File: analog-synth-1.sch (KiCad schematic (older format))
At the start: 0 parts

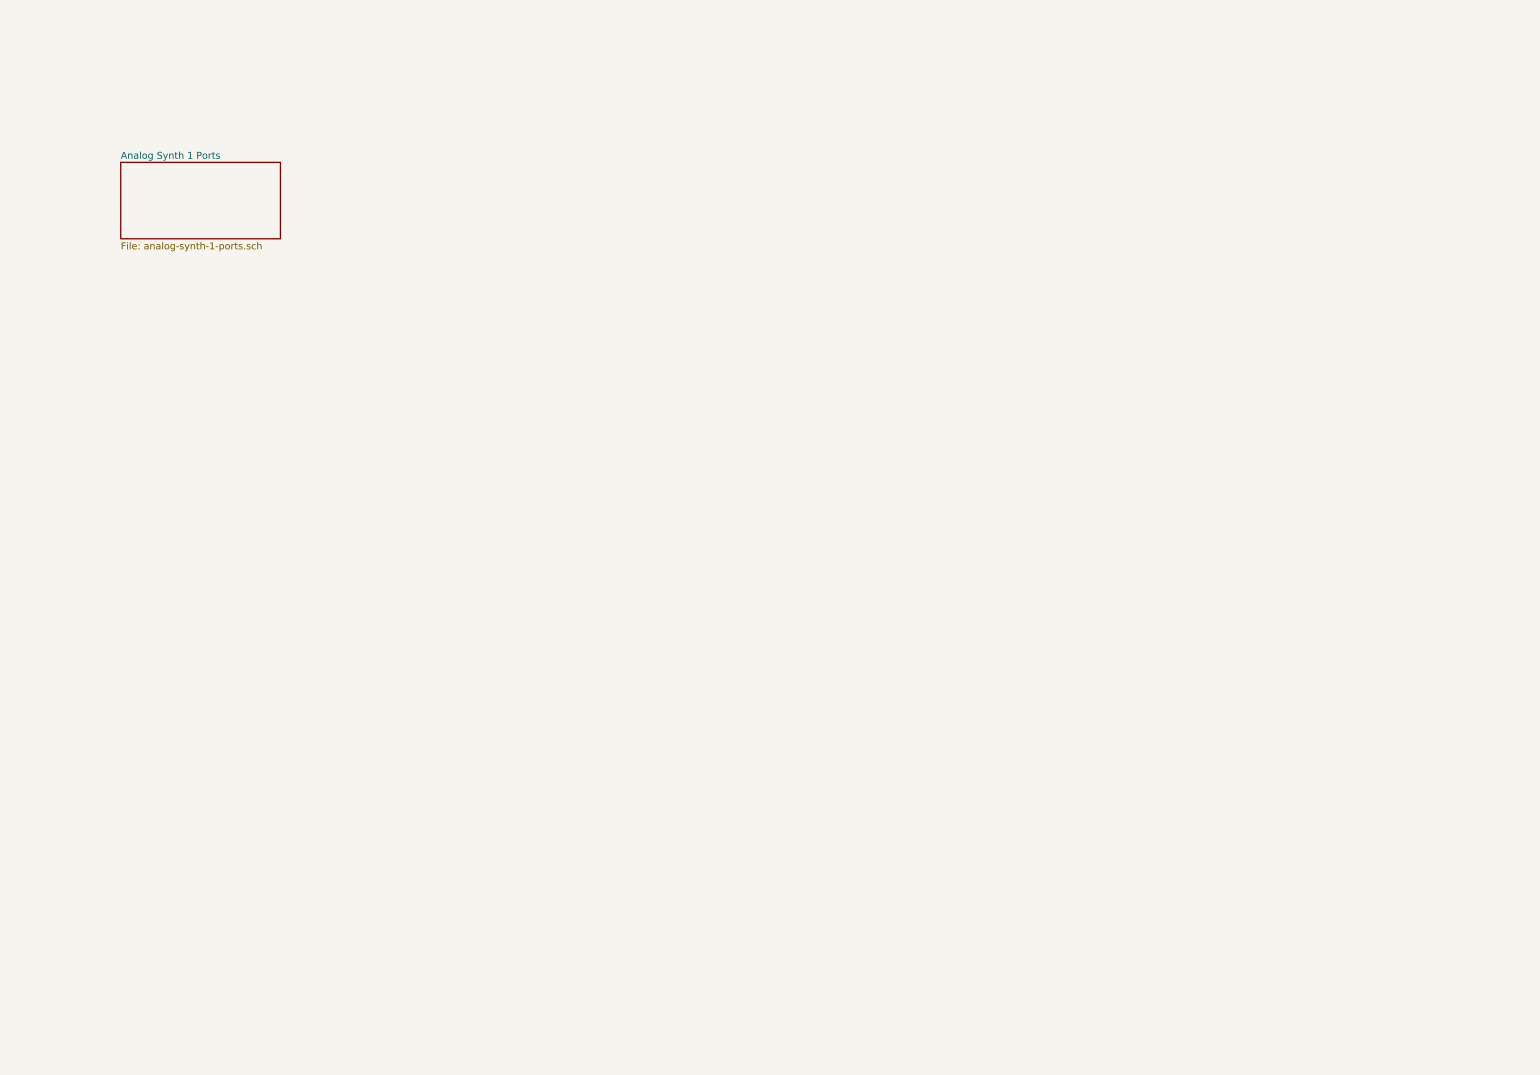
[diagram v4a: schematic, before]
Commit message: Finish basic synth circuit diagram
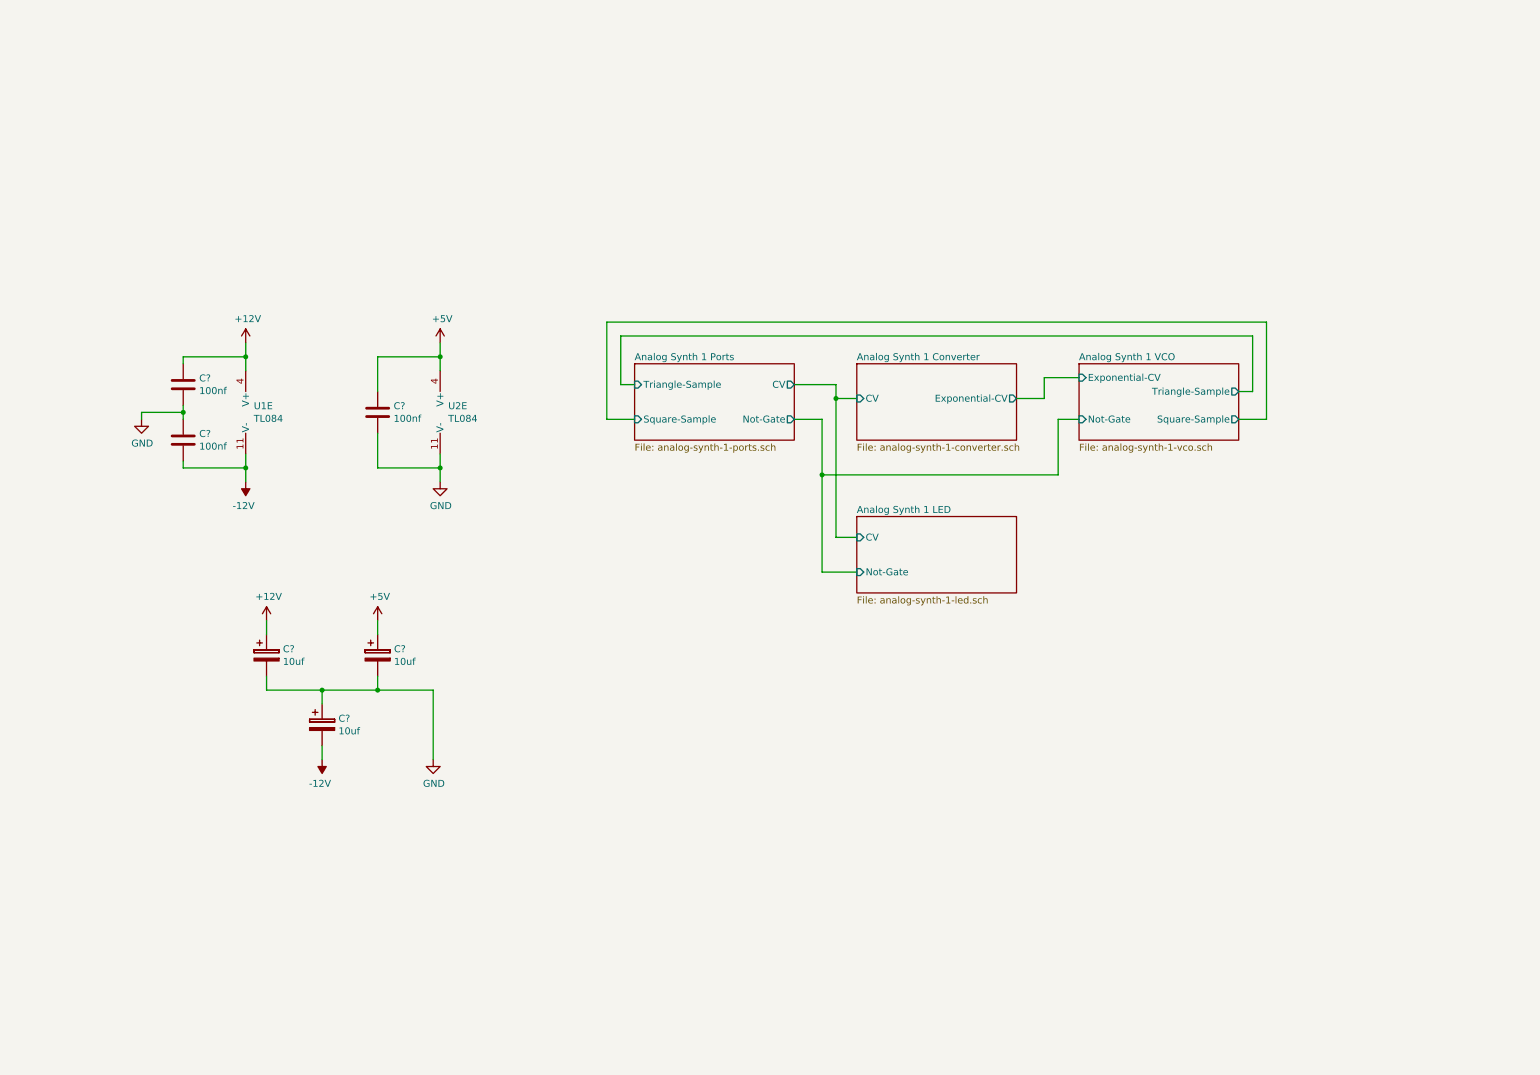
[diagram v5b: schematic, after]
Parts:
- added C? (x3): 100nf, symbol Device:C
- added C? (x3): 10uf, symbol Device:CP
- added U1, U2: TL084, symbol Amplifier_Operational:TL084
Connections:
- new net +12V: C?.1, C?.1, U1.4 (V+)
- new net +5V: C?.1, C?.1, U2.4 (V+)
- new net -12V: C?.2, C?.2, U1.11 (V-)
- new net GND: C?.1, C?.1, C?.2, C?.2, C?.2, C?.2, U2.11 (V-)

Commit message: Annotate components
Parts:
- gave numbers to parts that had none: 6
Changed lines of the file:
@@
 $EndComp
 $Comp
-L power:+12V #PWR?
+L power:+12V #PWR02
 U 1 1 5C8A06B3
 P 2250 2700
-F 0 "#PWR?" H 2250 2550 50  0001 C CNN
+F 0 "#PWR02" H 2250 2550 50  0001 C CNN
 F 1 "+12V" H 2265 2873 50  0000 C CNN
 F 2 "" H 2250 2700 50  0001 C CNN
@@
 	2250 2700 2250 2800
 $Comp
-L power:-12V #PWR?
+L power:-12V #PWR03
 U 1 1 5C8A0733
 P 2250 3700
-F 0 "#PWR?" H 2250 3800 50  0001 C CNN
+F 0 "#PWR03" H 2250 3800 50  0001 C CNN
 F 1 "-12V" H 2265 3873 50  0000 C CNN
 F 2 "" H 2250 3700 50  0001 C CNN
@@
 	2250 3700 2250 3600
 $Comp
-L power:GND #PWR?
+L power:GND #PWR09
 U 1 1 5C8A07A5
 P 3650 3700
-F 0 "#PWR?" H 3650 3450 50  0001 C CNN
+F 0 "#PWR09" H 3650 3450 50  0001 C CNN
 F 1 "GND" H 3655 3527 50  0000 C CNN
 F 2 "" H 3650 3700 50  0001 C CNN
@@
 $EndComp
 $Comp
-L power:+5V #PWR?
+L power:+5V #PWR08
 U 1 1 5C8A0819
 P 3650 2700
-F 0 "#PWR?" H 3650 2550 50  0001 C CNN
+F 0 "#PWR08" H 3650 2550 50  0001 C CNN
 F 1 "+5V" H 3665 2873 50  0000 C CNN
 F 2 "" H 3650 2700 50  0001 C CNN
@@
 $EndComp
 $Comp
-L Device:C C?
+L Device:C C1
 U 1 1 5C8A08B9
 P 1800 3000
-F 0 "C?" H 1915 3046 50  0000 L CNN
+F 0 "C1" H 1915 3046 50  0000 L CNN
 F 1 "100nf" H 1915 2955 50  0000 L CNN
 F 2 "" H 1838 2850 50  0001 C CNN
@@
 $EndComp
 $Comp
-L Device:C C?
+L Device:C C2
 U 1 1 5C8A08FC
 P 1800 3400
-F 0 "C?" H 1915 3446 50  0000 L CNN
+F 0 "C2" H 1915 3446 50  0000 L CNN
 F 1 "100nf" H 1915 3355 50  0000 L CNN
 F 2 "" H 1838 3250 50  0001 C CNN
@@
 	2250 3600 2250 3500
 $Comp
-L power:GND #PWR?
+L power:GND #PWR01
 U 1 1 5C8A0ABB
 P 1500 3250
-F 0 "#PWR?" H 1500 3000 50  0001 C CNN
+F 0 "#PWR01" H 1500 3000 50  0001 C CNN
 F 1 "GND" H 1505 3077 50  0000 C CNN
 F 2 "" H 1500 3250 50  0001 C CNN
@@
 	1800 3200 1800 3250
 $Comp
-L Device:C C?
+L Device:C C5
 U 1 1 5C8A0BD8
 P 3200 3200
-F 0 "C?" H 3315 3246 50  0000 L CNN
+F 0 "C5" H 3315 3246 50  0000 L CNN
 F 1 "100nf" H 3315 3155 50  0000 L CNN
 F 2 "" H 3238 3050 50  0001 C CNN
@@
 	3650 3600 3650 3700
 $Comp
-L power:+12V #PWR?
+L power:+12V #PWR04
 U 1 1 5C8A2596
 P 2400 4700
-F 0 "#PWR?" H 2400 4550 50  0001 C CNN
+F 0 "#PWR04" H 2400 4550 50  0001 C CNN
 F 1 "+12V" H 2415 4873 50  0000 C CNN
 F 2 "" H 2400 4700 50  0001 C CNN
@@
 $EndComp
 $Comp
-L power:+5V #PWR?
+L power:+5V #PWR06
 U 1 1 5C8A25DD
 P 3200 4700
-F 0 "#PWR?" H 3200 4550 50  0001 C CNN
+F 0 "#PWR06" H 3200 4550 50  0001 C CNN
 F 1 "+5V" H 3215 4873 50  0000 C CNN
 F 2 "" H 3200 4700 50  0001 C CNN
@@
 $EndComp
 $Comp
-L Device:CP C?
+L Device:CP C6
 U 1 1 5C8A292F
 P 3200 4950
-F 0 "C?" H 3318 4996 50  0000 L CNN
+F 0 "C6" H 3318 4996 50  0000 L CNN
 F 1 "10uf" H 3318 4905 50  0000 L CNN
 F 2 "" H 3238 4800 50  0001 C CNN
@@
 $EndComp
 $Comp
-L Device:CP C?
+L Device:CP C3
 U 1 1 5C8A2973
 P 2400 4950
-F 0 "C?" H 2518 4996 50  0000 L CNN
+F 0 "C3" H 2518 4996 50  0000 L CNN
 F 1 "10uf" H 2518 4905 50  0000 L CNN
 F 2 "" H 2438 4800 50  0001 C CNN
@@
 	3200 5200 3200 5100
 $Comp
-L Device:CP C?
+L Device:CP C4
 U 1 1 5C8A3250
 P 2800 5450
-F 0 "C?" H 2918 5496 50  0000 L CNN
+F 0 "C4" H 2918 5496 50  0000 L CNN
 F 1 "10uf" H 2918 5405 50  0000 L CNN
 F 2 "" H 2838 5300 50  0001 C CNN
@@
 	2800 5200 3200 5200
 $Comp
-L power:-12V #PWR?
+L power:-12V #PWR05
 U 1 1 5C8A3697
 P 2800 5700
-F 0 "#PWR?" H 2800 5800 50  0001 C CNN
+F 0 "#PWR05" H 2800 5800 50  0001 C CNN
 F 1 "-12V" H 2815 5873 50  0000 C CNN
 F 2 "" H 2800 5700 50  0001 C CNN
@@
 	2800 5700 2800 5600
 $Comp
-L power:GND #PWR?
+L power:GND #PWR07
 U 1 1 5C8A3B5D
 P 3600 5700
-F 0 "#PWR?" H 3600 5450 50  0001 C CNN
+F 0 "#PWR07" H 3600 5450 50  0001 C CNN
 F 1 "GND" H 3605 5527 50  0000 C CNN
 F 2 "" H 3600 5700 50  0001 C CNN

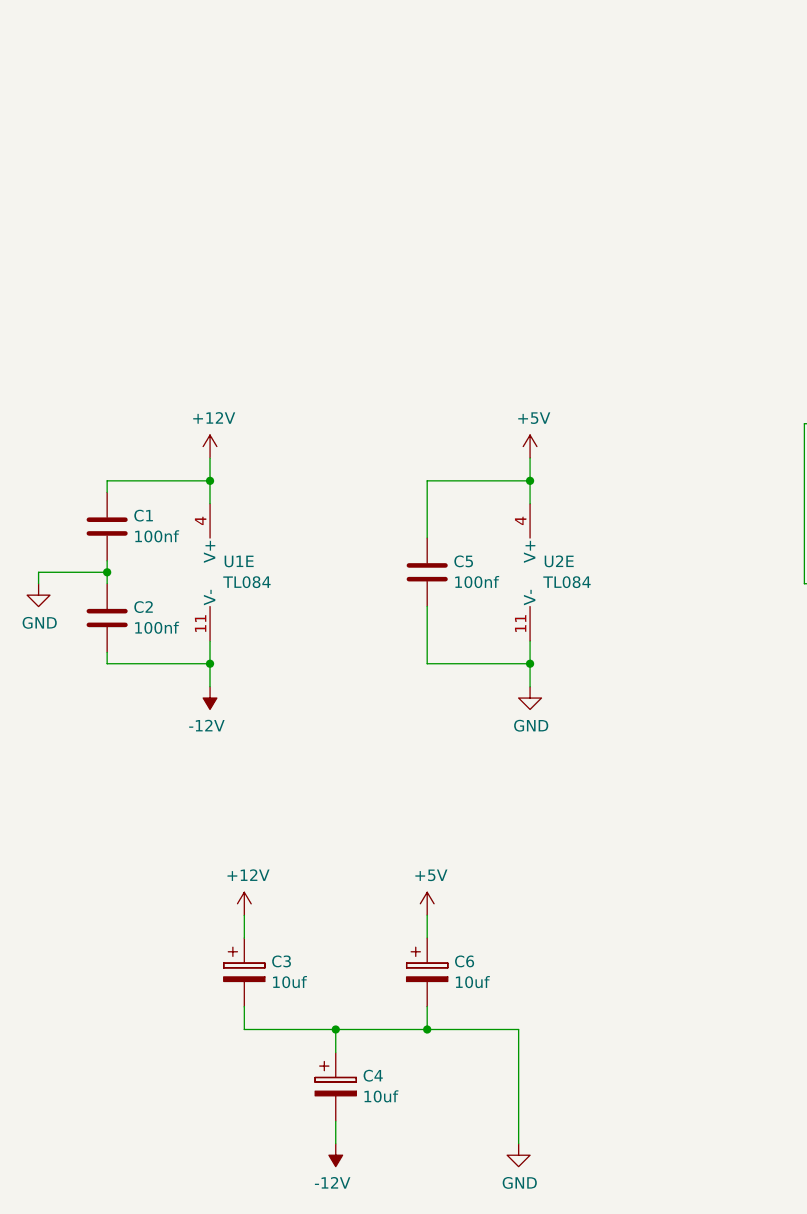
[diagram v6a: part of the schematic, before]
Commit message: Add ATtiny85 overdrive protection, fix #5
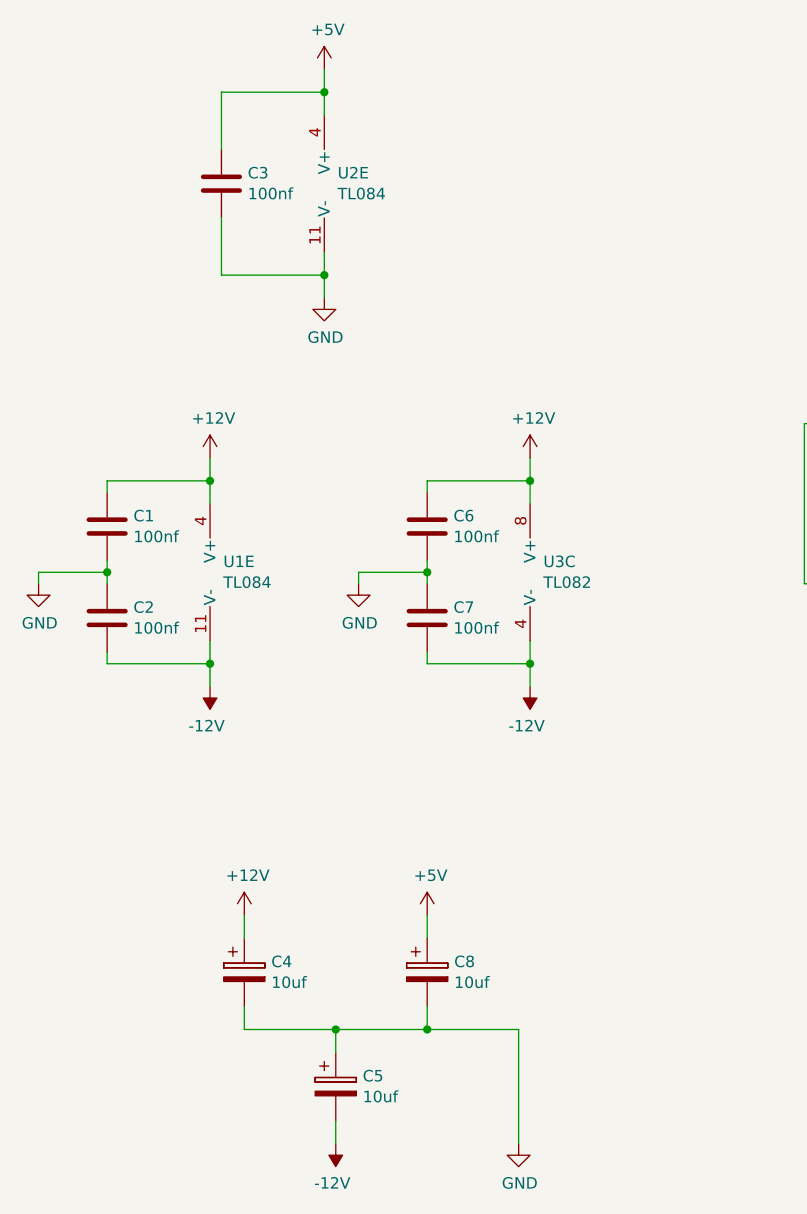
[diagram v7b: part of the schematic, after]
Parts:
- added C6, C7: 100nf, symbol Device:C
- added U3: TL082, symbol Amplifier_Operational:TL082
- renumbered C5 to C3, C3 to C4, C4 to C5, C6 to C8
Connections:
- net +12V: now also C6.1, U3.8 (V+)
- net -12V: now also C7.2, U3.4 (V-)
- net GND: now also C6.2, C7.1
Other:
- moved on the sheet: C3, U2E
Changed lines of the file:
@@
 L Amplifier_Operational:TL084 U2
 U 5 1 5C8A05FF
-P 3750 3200
-F 0 "U2" H 3708 3246 50  0000 L CNN
-F 1 "TL084" H 3708 3155 50  0000 L CNN
-F 2 "" H 3700 3300 50  0001 C CNN
-F 3 "http://www.ti.com/lit/ds/symlink/tl081.pdf" H 3800 3400 50  0001 C CNN
-	5    3750 3200
+P 2850 1500
+F 0 "U2" H 2808 1546 50  0000 L CNN
+F 1 "TL084" H 2808 1455 50  0000 L CNN
+F 2 "" H 2800 1600 50  0001 C CNN
+F 3 "http://www.ti.com/lit/ds/symlink/tl081.pdf" H 2900 1700 50  0001 C CNN
+	5    2850 1500
 	1    0    0    -1
 $EndComp
@@
 	2250 3700 2250 3600
 $Comp
-L power:GND #PWR09
+L power:GND #PWR06
 U 1 1 5C8A07A5
-P 3650 3700
-F 0 "#PWR09" H 3650 3450 50  0001 C CNN
-F 1 "GND" H 3655 3527 50  0000 C CNN
-F 2 "" H 3650 3700 50  0001 C CNN
-F 3 "" H 3650 3700 50  0001 C CNN
-	1    3650 3700
-	1    0    0    -1
-$EndComp
-$Comp
-L power:+5V #PWR08
+P 2750 2000
+F 0 "#PWR06" H 2750 1750 50  0001 C CNN
+F 1 "GND" H 2755 1827 50  0000 C CNN
+F 2 "" H 2750 2000 50  0001 C CNN
+F 3 "" H 2750 2000 50  0001 C CNN
+	1    2750 2000
+	1    0    0    -1
+$EndComp
+$Comp
+L power:+5V #PWR05
 U 1 1 5C8A0819
-P 3650 2700
-F 0 "#PWR08" H 3650 2550 50  0001 C CNN
-F 1 "+5V" H 3665 2873 50  0000 C CNN
-F 2 "" H 3650 2700 50  0001 C CNN
-F 3 "" H 3650 2700 50  0001 C CNN
-	1    3650 2700
+P 2750 1000
+F 0 "#PWR05" H 2750 850 50  0001 C CNN
+F 1 "+5V" H 2765 1173 50  0000 C CNN
+F 2 "" H 2750 1000 50  0001 C CNN
+F 3 "" H 2750 1000 50  0001 C CNN
+	1    2750 1000
 	1    0    0    -1
 $EndComp
@@
 	1800 3200 1800 3250
 $Comp
-L Device:C C5
+L Device:C C3
 U 1 1 5C8A0BD8
-P 3200 3200
-F 0 "C5" H 3315 3246 50  0000 L CNN
-F 1 "100nf" H 3315 3155 50  0000 L CNN
-F 2 "" H 3238 3050 50  0001 C CNN
-F 3 "~" H 3200 3200 50  0001 C CNN
-	1    3200 3200
-	1    0    0    -1
-$EndComp
-Wire Wire Line
-	3200 3050 3200 2800
-Wire Wire Line
-	3200 3350 3200 3600
-Wire Wire Line
-	3650 2700 3650 2800
-Wire Wire Line
-	3650 3500 3650 3600
-Wire Wire Line
-	3650 2800 3200 2800
-Connection ~ 3650 2800
-Wire Wire Line
-	3650 2800 3650 2900
-Wire Wire Line
-	3650 3600 3200 3600
-Connection ~ 3650 3600
-Wire Wire Line
-	3650 3600 3650 3700
+P 2300 1500
+F 0 "C3" H 2415 1546 50  0000 L CNN
+F 1 "100nf" H 2415 1455 50  0000 L CNN
+F 2 "" H 2338 1350 50  0001 C CNN
+F 3 "~" H 2300 1500 50  0001 C CNN
+	1    2300 1500
+	1    0    0    -1
+$EndComp
+Wire Wire Line
+	2300 1350 2300 1100
+Wire Wire Line
+	2300 1650 2300 1900
+Wire Wire Line
+	2750 1000 2750 1100
+Wire Wire Line
+	2750 1800 2750 1900
+Wire Wire Line
+	2750 1100 2300 1100
+Connection ~ 2750 1100
+Wire Wire Line
+	2750 1100 2750 1200
+Wire Wire Line
+	2750 1900 2300 1900
+Connection ~ 2750 1900
+Wire Wire Line
+	2750 1900 2750 2000
 $Comp
 L power:+12V #PWR04
@@
 $EndComp
 $Comp
-L power:+5V #PWR06
+L power:+5V #PWR09
 U 1 1 5C8A25DD
 P 3200 4700
-F 0 "#PWR06" H 3200 4550 50  0001 C CNN
+F 0 "#PWR09" H 3200 4550 50  0001 C CNN
 F 1 "+5V" H 3215 4873 50  0000 C CNN
 F 2 "" H 3200 4700 50  0001 C CNN
@@
 $EndComp
 $Comp
-L Device:CP C6
+L Device:CP C8
 U 1 1 5C8A292F
 P 3200 4950
-F 0 "C6" H 3318 4996 50  0000 L CNN
+F 0 "C8" H 3318 4996 50  0000 L CNN
 F 1 "10uf" H 3318 4905 50  0000 L CNN
 F 2 "" H 3238 4800 50  0001 C CNN
@@
 $EndComp
 $Comp
-L Device:CP C3
+L Device:CP C4
 U 1 1 5C8A2973
 P 2400 4950
-F 0 "C3" H 2518 4996 50  0000 L CNN
+F 0 "C4" H 2518 4996 50  0000 L CNN
 F 1 "10uf" H 2518 4905 50  0000 L CNN
 F 2 "" H 2438 4800 50  0001 C CNN
@@
 	3200 5200 3200 5100
 $Comp
-L Device:CP C4
+L Device:CP C5
 U 1 1 5C8A3250
 P 2800 5450
-F 0 "C4" H 2918 5496 50  0000 L CNN
+F 0 "C5" H 2918 5496 50  0000 L CNN
 F 1 "10uf" H 2918 5405 50  0000 L CNN
 F 2 "" H 2838 5300 50  0001 C CNN
@@
 	2800 5200 3200 5200
 $Comp
-L power:-12V #PWR05
+L power:-12V #PWR07
 U 1 1 5C8A3697
 P 2800 5700
-F 0 "#PWR05" H 2800 5800 50  0001 C CNN
+F 0 "#PWR07" H 2800 5800 50  0001 C CNN
 F 1 "-12V" H 2815 5873 50  0000 C CNN
 F 2 "" H 2800 5700 50  0001 C CNN
@@
 	2800 5700 2800 5600
 $Comp
-L power:GND #PWR07
+L power:GND #PWR010
 U 1 1 5C8A3B5D
 P 3600 5700
-F 0 "#PWR07" H 3600 5450 50  0001 C CNN
+F 0 "#PWR010" H 3600 5450 50  0001 C CNN
 F 1 "GND" H 3605 5527 50  0000 C CNN
 F 2 "" H 3600 5700 50  0001 C CNN
@@
 	6400 4350 6650 4350
 Connection ~ 6400 3650
+$Comp
+L power:+12V #PWR011
+U 1 1 5CA1F7C2
+P 3650 2700
+F 0 "#PWR011" H 3650 2550 50  0001 C CNN
+F 1 "+12V" H 3665 2873 50  0000 C CNN
+F 2 "" H 3650 2700 50  0001 C CNN
+F 3 "" H 3650 2700 50  0001 C CNN
+	1    3650 2700
+	1    0    0    -1
+$EndComp
+Wire Wire Line
+	3650 2700 3650 2800
+$Comp
+L power:-12V #PWR012
+U 1 1 5CA1F7C9
+P 3650 3700
+F 0 "#PWR012" H 3650 3800 50  0001 C CNN
+F 1 "-12V" H 3665 3873 50  0000 C CNN
+F 2 "" H 3650 3700 50  0001 C CNN
+F 3 "" H 3650 3700 50  0001 C CNN
+	1    3650 3700
+	-1   0    0    1
+$EndComp
+Wire Wire Line
+	3650 3700 3650 3600
+$Comp
+L Device:C C6
+U 1 1 5CA1F7D0
+P 3200 3000
+F 0 "C6" H 3315 3046 50  0000 L CNN
+F 1 "100nf" H 3315 2955 50  0000 L CNN
+F 2 "" H 3238 2850 50  0001 C CNN
+F 3 "~" H 3200 3000 50  0001 C CNN
+	1    3200 3000
+	1    0    0    -1
+$EndComp
+$Comp
+L Device:C C7
+U 1 1 5CA1F7D7
+P 3200 3400
+F 0 "C7" H 3315 3446 50  0000 L CNN
+F 1 "100nf" H 3315 3355 50  0000 L CNN
+F 2 "" H 3238 3250 50  0001 C CNN
+F 3 "~" H 3200 3400 50  0001 C CNN
+	1    3200 3400
+	1    0    0    -1
+$EndComp
+Wire Wire Line
+	3650 2800 3200 2800
+Wire Wire Line
+	3200 2800 3200 2850
+Connection ~ 3650 2800
+Wire Wire Line
+	3650 2800 3650 2900
+Wire Wire Line
+	3200 3150 3200 3200
+Wire Wire Line
+	3200 3550 3200 3600
+Wire Wire Line
+	3200 3600 3650 3600
+Connection ~ 3650 3600
+Wire Wire Line
+	3650 3600 3650 3500
+$Comp
+L power:GND #PWR08
+U 1 1 5CA1F7E7
+P 2900 3250
+F 0 "#PWR08" H 2900 3000 50  0001 C CNN
+F 1 "GND" H 2905 3077 50  0000 C CNN
+F 2 "" H 2900 3250 50  0001 C CNN
+F 3 "" H 2900 3250 50  0001 C CNN
+	1    2900 3250
+	1    0    0    -1
+$EndComp
+Wire Wire Line
+	2900 3250 2900 3200
+Wire Wire Line
+	2900 3200 3200 3200
+Connection ~ 3200 3200
+Wire Wire Line
+	3200 3200 3200 3250
+$Comp
+L Amplifier_Operational:TL082 U3
+U 3 1 5CA21A90
+P 3750 3200
+F 0 "U3" H 3708 3246 50  0000 L CNN
+F 1 "TL082" H 3708 3155 50  0000 L CNN
+F 2 "" H 3750 3200 50  0001 C CNN
+F 3 "http://www.ti.com/lit/ds/symlink/tl081.pdf" H 3750 3200 50  0001 C CNN
+	3    3750 3200
+	1    0    0    -1
+$EndComp
 $EndSCHEMATC
